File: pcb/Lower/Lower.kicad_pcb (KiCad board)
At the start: 2 copper layers, 52 x 40 mm, 35 parts, among them J1 AudioJack3, J2 AudioJack3, J3 Barrel_Jack, J4 Conn_01x04, Q1 AO3401A, SW1 SW_Push_3PDT, U1 TL072

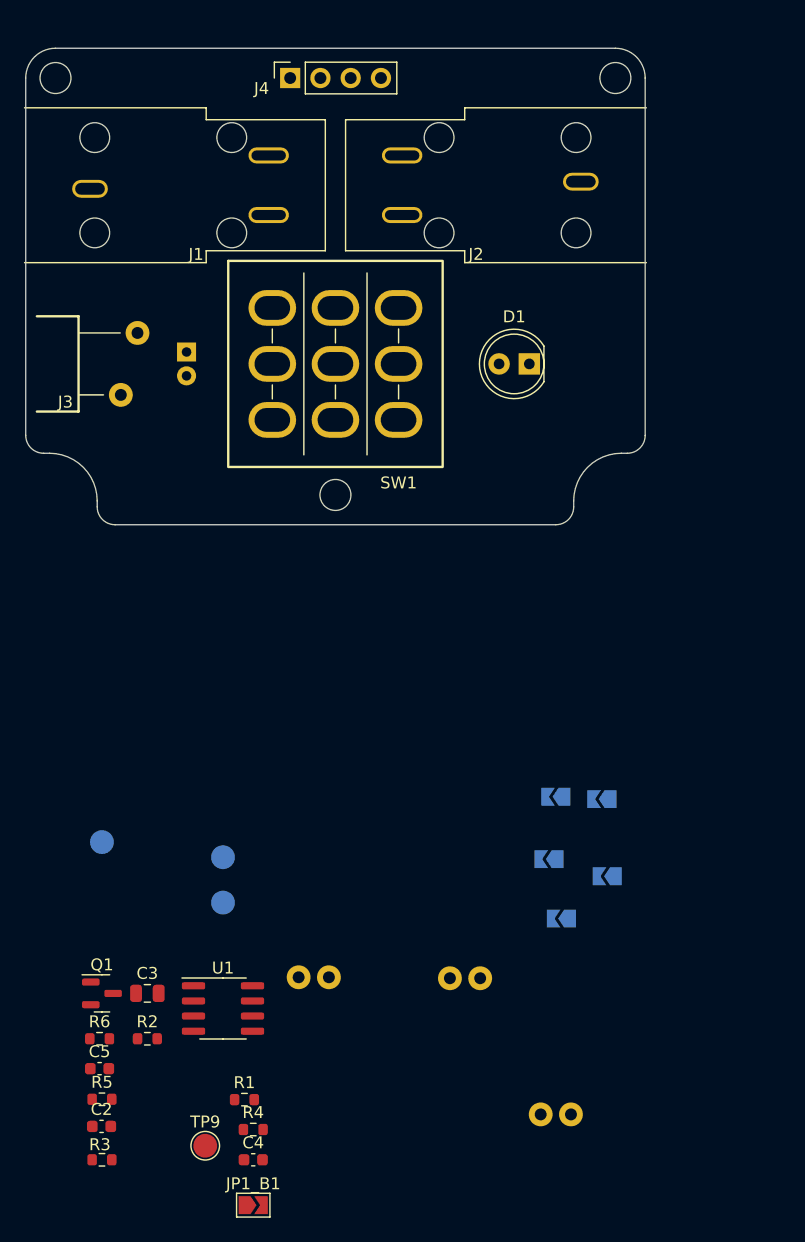
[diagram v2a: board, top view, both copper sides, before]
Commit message: [Lower] Fix LED wiring in Schematic, route whole board
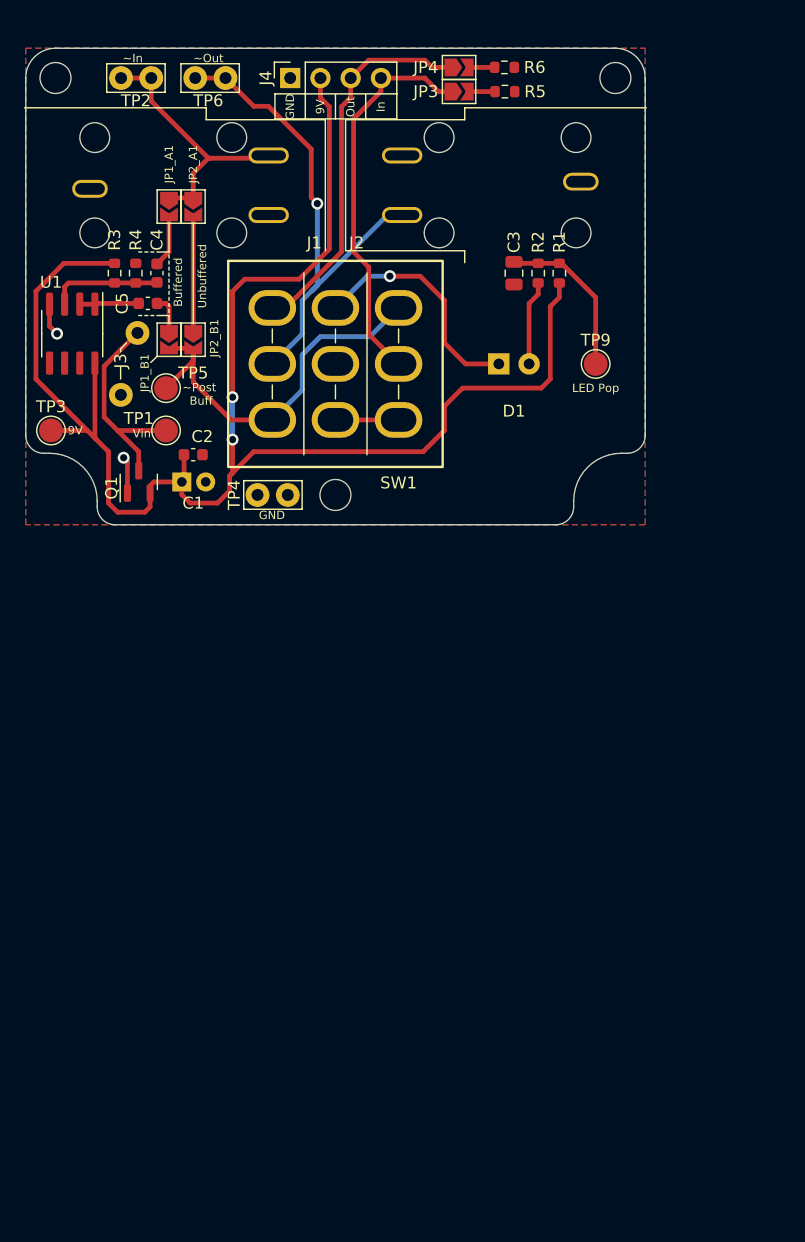
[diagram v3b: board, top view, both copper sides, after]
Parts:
- JP1_A1, JP2_A1, JP2_B1, JP3, JP4, TP1, TP2, TP3, TP4, TP5, TP6: moved to F.Cu
- moved R5 91.1 mm to (163.7, 85.6), turned to 180 degrees
- moved R6 88.3 mm to (163.7, 83.6), turned to 180 degrees
- moved TP2 81.4 mm to (131.5, 84.5), turned to 0 degrees
- moved TP6 76.3 mm to (137.7, 84.5), turned to 0 degrees
- moved C4 74.9 mm to (134.5, 100.9), turned to -90 degrees
- moved R3 74.4 mm to (131.0, 100.9), turned to -90 degrees
- moved R1 74.2 mm to (168.3, 100.9), turned to 90 degrees
- moved TP9 73.4 mm to (171.3, 108.5)
- moved JP1_B1 73.0 mm to (135.5, 106.5), turned to -90 degrees
- moved R4 72.6 mm to (132.7, 100.9), turned to 90 degrees
- moved R2 72.2 mm to (166.5, 100.9), turned to -90 degrees
- moved JP1_A1 68.2 mm to (135.5, 95.3), turned to -90 degrees
- moved C3 67.8 mm to (164.5, 100.9), turned to -90 degrees
- moved JP3 67.0 mm to (159.9, 85.6), turned to 0 degrees
- moved C5 64.4 mm to (133.8, 103.4)
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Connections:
- JP1_B1 pad 2: Net-(D1-Pad1) -> Net-(JP1_B1-Pad2)
- JP2_B1 pad 2: Net-(D1-Pad1) -> Net-(JP1_B1-Pad2)
- SW1 pad 1: Net-(D1-Pad1) -> Net-(JP1_B1-Pad2)
- SW1 pad 9: Net-(D1-Pad1) -> Net-(JP1_B1-Pad2)
- TP5 pad 1: Net-(D1-Pad1) -> Net-(JP1_B1-Pad2)
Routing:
- net +9V: track 0.00 -> 135.0 mm, vias 0 -> 2
- net /Output: track 0.00 -> 43.2 mm, vias 0 -> 1
- net Net-(JP1_B1-Pad2): track 0.00 -> 33.4 mm
- net Upper_PCB_Output: track 0.00 -> 33.3 mm
- net Upper_PCB_Input: track 0.00 -> 33.1 mm
- net /Input: track 0.00 -> 23.5 mm
- net Net-(D1-Pad1): track 0.00 -> 20.8 mm, vias 0 -> 1
- net Net-(J3-Pad2): track 0.00 -> 18.0 mm
- net Net-(C3-Pad1): track 0.00 -> 13.7 mm
- net Net-(JP2_A1-Pad2): track 0.00 -> 9.73 mm
- net Net-(C4-Pad2): track 0.00 -> 9.36 mm
- net Net-(D1-Pad2): track 0.00 -> 7.11 mm
- net GND: track 0.00 -> 5.84 mm, vias 0 -> 2
- net Net-(SW1-Pad3): track 0.00 -> 5.30 mm
- net Net-(C5-Pad1): track 0.00 -> 4.97 mm
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- added copper zone on B.Cu, net GND
- added copper zone on F.Cu, net GND
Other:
- board text added: "9V"
- board text added: "Buffered"
- board text added: "GND"
- board text added: "In"
- board text added: "LED Pop"
- board text added: "Out"
- board text added: "Unbuffered"
- board text added: "Vin"
- board text added: "~In"
- board text added: "~Out"
- board text added: "~Post Buff"
